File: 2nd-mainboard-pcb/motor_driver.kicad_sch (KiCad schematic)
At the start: 15 parts, among them J10 Servo Motor BL Touch, J11 T3, J7 Stepper Motor, J8 Servo Motor SM, J9 Microstepping, U11 TMC2209_SILENTSTEPSTICK, U12 MPU-6050

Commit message: Testpoints hinzugefügt
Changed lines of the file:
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@@
 	(wire
 		(pts
-			(xy 67.31 81.28) (xy 60.96 81.28)
+			(xy 64.77 80.01) (xy 60.96 80.01)
 		)
 		(stroke
@@
 	(wire
 		(pts
-			(xy 67.31 81.28) (xy 67.31 82.55)
+			(xy 64.77 80.01) (xy 64.77 81.28)
 		)
 		(stroke
@@
 		(pts
 			(xy 128.27 105.41) (xy 128.27 111.76)
-		)
-		(stroke
-			(width 0)
-			(type default)
-		)
-	)
-	(wire
-		(pts
-			(xy 60.96 81.28) (xy 60.96 80.01)
 		)
 		(stroke
@@
 	(symbol
 		(lib_id "power:GND")
-		(at 67.31 82.55 0)
+		(at 64.77 81.28 0)
 		(unit 1)
 		(exclude_from_sim no)
@@
 		(fields_autoplaced yes)
 		(property "Reference" "#PWR056"
-			(at 67.31 88.9 0)
+			(at 64.77 87.63 0)
 			(effects
 				(font
@@
 		)
 		(property "Value" "GND"
-			(at 67.31 87.63 0)
+			(at 64.77 86.36 0)
 			(effects
 				(font
@@
 		)
 		(property "Footprint" ""
-			(at 67.31 82.55 0)
+			(at 64.77 81.28 0)
 			(effects
 				(font
@@
 		)
 		(property "Datasheet" ""
-			(at 67.31 82.55 0)
+			(at 64.77 81.28 0)
 			(effects
 				(font
@@
 		)
 		(property "Description" "Power symbol creates a global label with name \"GND\" , ground"
-			(at 67.31 82.55 0)
-			(effects
-				(font
+			(at 64.77 81.28 0)
+			(effects
+				(font

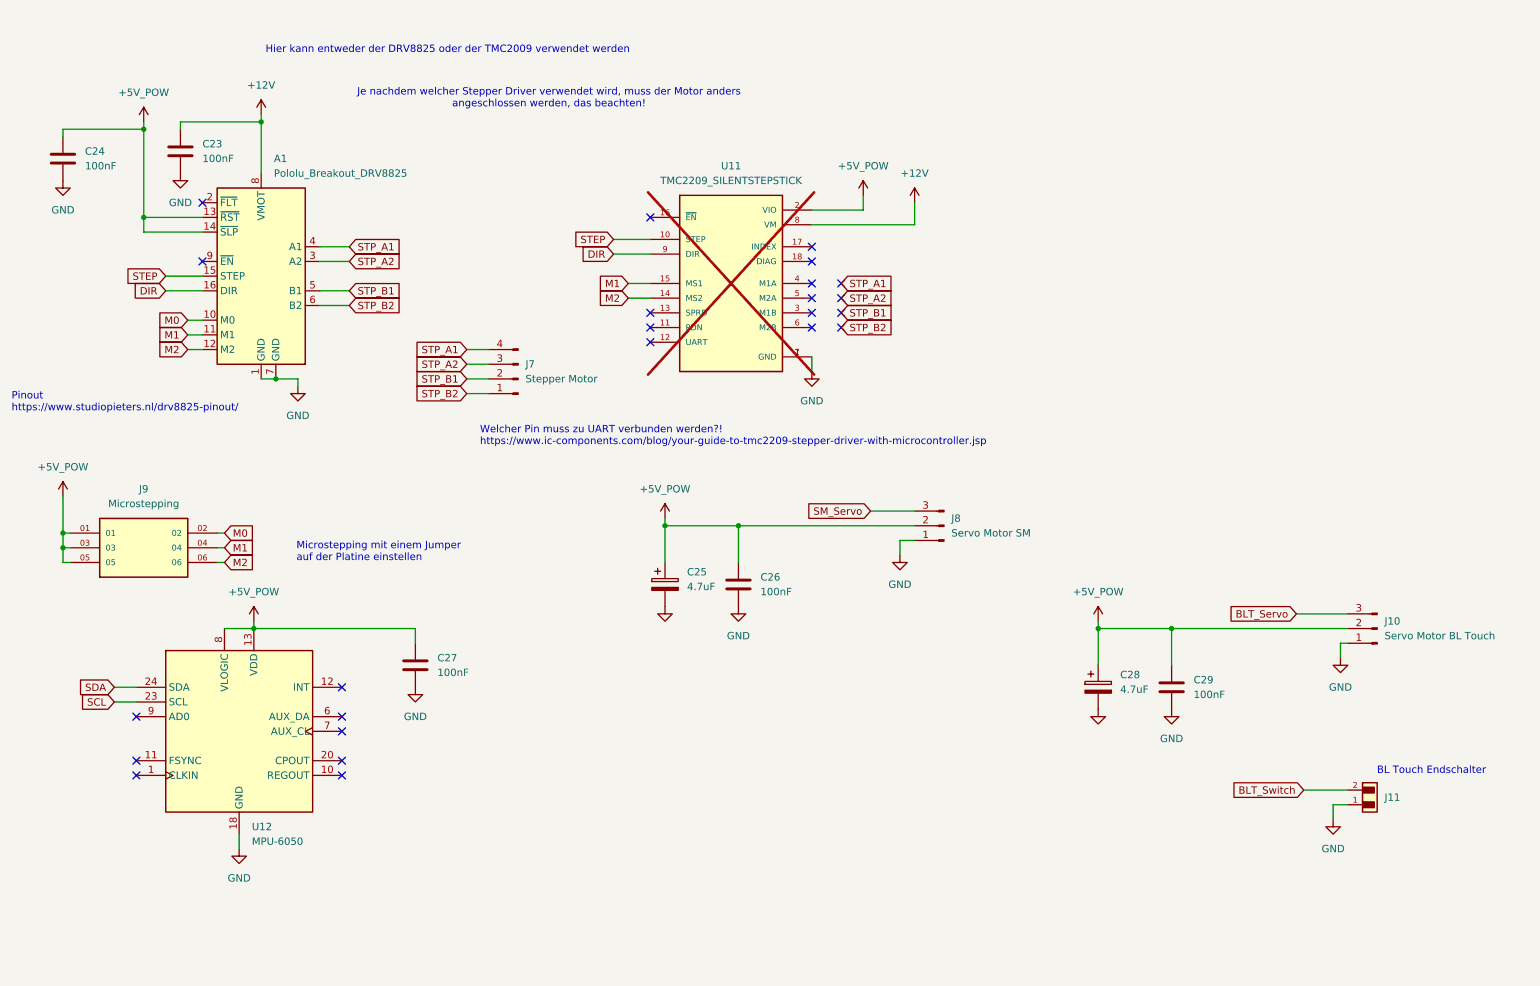
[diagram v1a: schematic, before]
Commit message: updated a bit of the track widths, removed comments in schematic
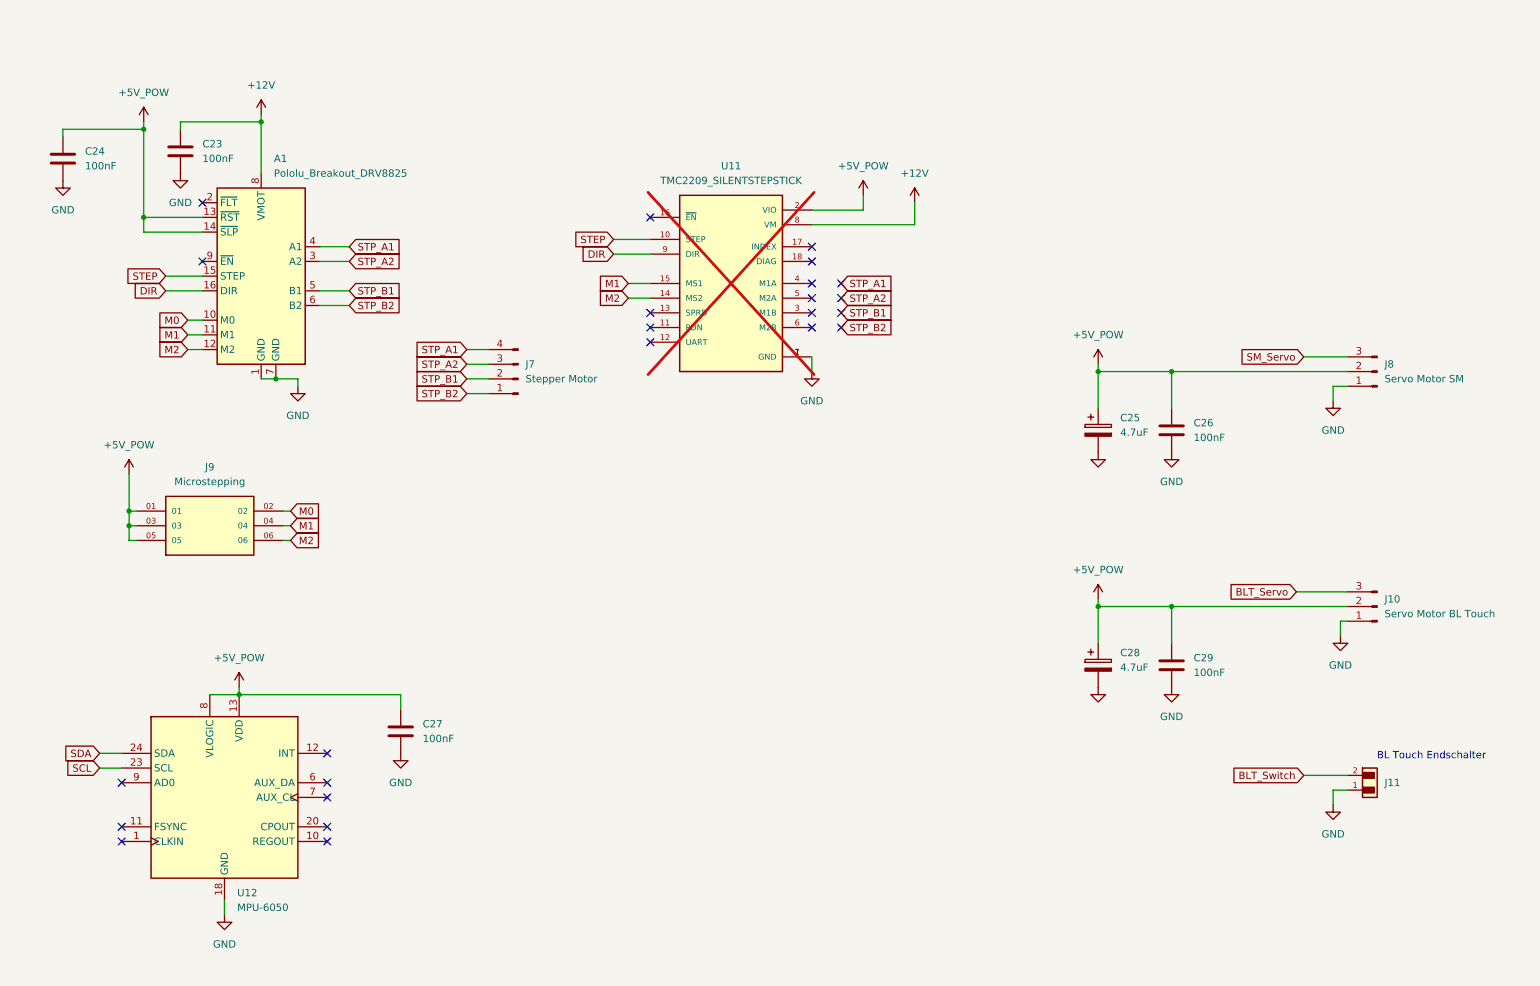
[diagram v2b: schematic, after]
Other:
- note removed: "Hier kann entweder der DRV8825 oder der TMC2009 verwendet werden"
- note removed: "Je nachdem welcher Stepper Driver verwendet wird, muss der Motor anders angeschlossen werden, das beachten!"
- note removed: "Microstepping mit einem Jumper auf der Platine einstellen"
- note removed: "Pinout https://www.studiopieters.nl/drv8825-pinout/"
- note removed: "Welcher Pin muss zu UART verbunden werden?! https://www.ic-components.com/blog/your-guide-to-tmc2209-stepper-driver-with-microcontroller.jsp"
- moved on the sheet: C25, C26, C27, C28, C29, J10, J11, J8, J9, U12

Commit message: cad files gebastelt
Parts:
- A1: footprint Module:Pololu_Breakout-16_15.2x20.3mm -> Imported_Component_Footprints:drv8825
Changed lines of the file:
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@@
 			)
 		)
-		(property "Footprint" "Module:Pololu_Breakout-16_15.2x20.3mm"
+		(property "Footprint" "Imported_Component_Footprints:drv8825"
 			(at 63.5 80.01 0)
 			(effects

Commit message: stacked pcb reworked
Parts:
- removed C24: 100nF, Capacitor_SMD:C_0402_1005Metric_Pad0.74x0.62mm_HandSolder, symbol Device:C
- removed U11: TMC2209_SILENTSTEPSTICK, Imported_Component_Footprints:MODULE_TMC2209_SILENTSTEPSTICK, symbol Imported_Component_Symbols:TMC2209_SILENTSTEPSTICK
- added C34: 10µF, Capacitor_SMD:C_0805_2012Metric_Pad1.18x1.45mm_HandSolder, symbol Device:C
- added C35: 100nF, Capacitor_SMD:C_0402_1005Metric_Pad0.74x0.62mm_HandSolder, symbol Device:C
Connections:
- net +5V_POW: no longer A1.13 (~{RST}), A1.14 (~{SLP}), U12.8 (VLOGIC)
- net GND: now also C34.2, C35.2
- new net +5V_USBC: C34.1, C35.1, U12.8 (VLOGIC)
- new net RESET: A1.13 (~{RST}), A1.14 (~{SLP})
- no-connect marks 24 -> 10
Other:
- moved on the sheet: A1, C23, C25, C26, C27, C28, C29, J10, J11, J7, J8, J9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

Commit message: rearragned componentens
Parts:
- C23, C26, C27, C29, C35: footprint Capacitor_SMD:C_0402_1005Metric_Pad0.74x0.62mm_HandSolder -> Capacitor_SMD:C_0603_1608Metric_Pad1.08x0.95mm_HandSolder
- C28: footprint Capacitor_SMD:C_0805_2012Metric_Pad1.18x1.45mm_HandSolder -> Capacitor_SMD:C_0603_1608Metric_Pad1.08x0.95mm_HandSolder
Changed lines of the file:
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@@
 			)
 		)
-		(property "Footprint" "Capacitor_SMD:C_0402_1005Metric_Pad0.74x0.62mm_HandSolder"
+		(property "Footprint" "Capacitor_SMD:C_0603_1608Metric_Pad1.08x0.95mm_HandSolder"
 			(at 261.3152 53.34 0)
 			(effects
@@
 			)
 		)
-		(property "Footprint" "Capacitor_SMD:C_0402_1005Metric_Pad0.74x0.62mm_HandSolder"
+		(property "Footprint" "Capacitor_SMD:C_0603_1608Metric_Pad1.08x0.95mm_HandSolder"
 			(at 219.4052 53.34 0)
 			(effects
@@
 			)
 		)
-		(property "Footprint" "Capacitor_SMD:C_0402_1005Metric_Pad0.74x0.62mm_HandSolder"
+		(property "Footprint" "Capacitor_SMD:C_0603_1608Metric_Pad1.08x0.95mm_HandSolder"
 			(at 46.6852 156.21 0)
 			(effects
@@
 			)
 		)
-		(property "Footprint" "Capacitor_SMD:C_0805_2012Metric_Pad1.18x1.45mm_HandSolder"
+		(property "Footprint" "Capacitor_SMD:C_0603_1608Metric_Pad1.08x0.95mm_HandSolder"
 			(at 33.9852 156.21 0)
 			(effects
@@
 			)
 		)
-		(property "Footprint" "Capacitor_SMD:C_0402_1005Metric_Pad0.74x0.62mm_HandSolder"
+		(property "Footprint" "Capacitor_SMD:C_0603_1608Metric_Pad1.08x0.95mm_HandSolder"
 			(at 82.2452 33.02 0)
 			(effects
@@
 			)
 		)
-		(property "Footprint" "Capacitor_SMD:C_0402_1005Metric_Pad0.74x0.62mm_HandSolder"
+		(property "Footprint" "Capacitor_SMD:C_0603_1608Metric_Pad1.08x0.95mm_HandSolder"
 			(at 47.9552 120.65 0)
 			(effects
